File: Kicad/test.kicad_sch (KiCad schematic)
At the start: 21 parts, among them J14 TEST POINTS

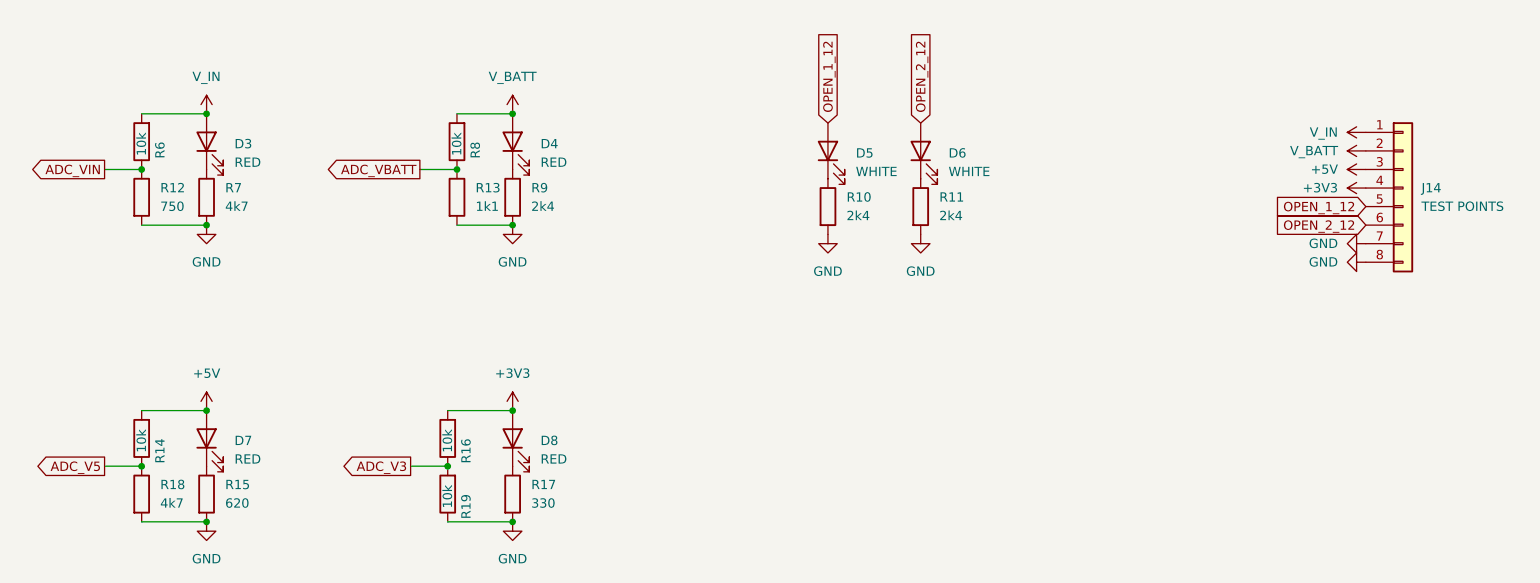
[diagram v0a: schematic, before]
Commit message: Rework of power circuits to improve protection
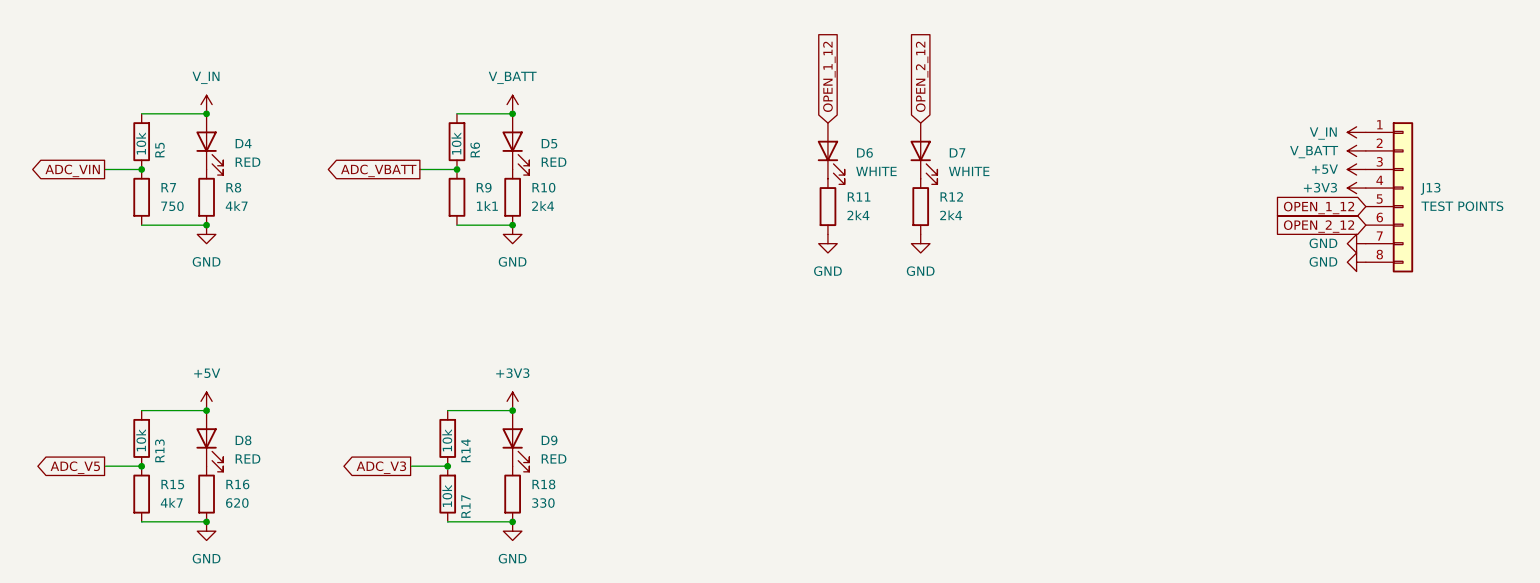
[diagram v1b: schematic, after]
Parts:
- renumbered D3 to D4, D4 to D5, D5 to D6, D6 to D7, D7 to D8, D8 to D9, J14 to J13, R9 to R10, R10 to R11, R11 to R12, R14 to R13, R16 to R14, R18 to R15, R15 to R16, R19 to R17, R17 to R18, R6 to R5, R8 to R6, R12 to R7, R7 to R8, R13 to R9
